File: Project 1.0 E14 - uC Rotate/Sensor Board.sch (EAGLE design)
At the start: 93 parts, among them IC1 LT1963EST-1.5, IC2 LT1963EST-1.5, IC4 LT1963EST-1.5

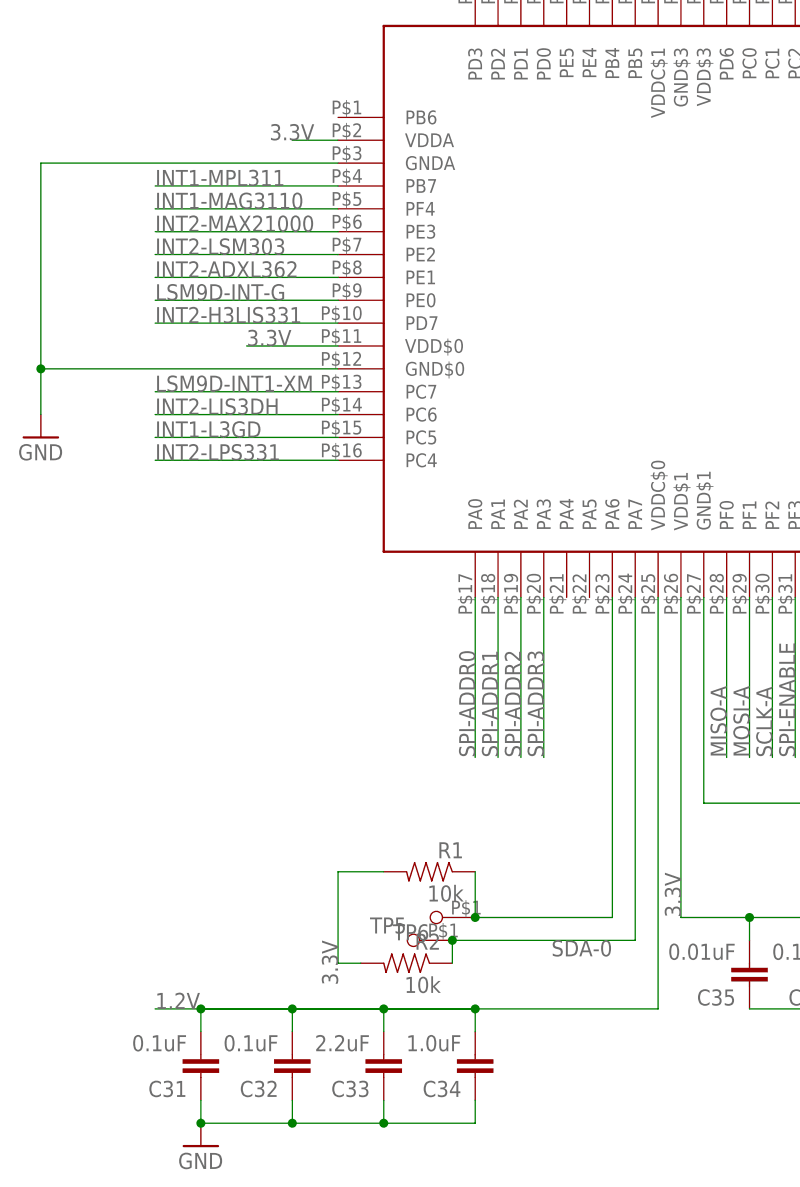
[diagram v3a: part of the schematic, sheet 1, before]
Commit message: All signal connections have been completed. Space has been adequately left between traces to allow for GND plane fill in. Power and GND have not been connected and signal and power trace widths have not been finalised. LSM9DS0 interrupts have not been finalised and may have been incorrectly connected.  LSM9DS0 Gyroscope data enable pin has not been connected since currently it is not clear what its use is or how it is to be used. Gyroscope programmable interrupt pin has been connected but the desired connection may be the gyroscope data ready pin. Also currently there appears to be no interrupt for the magnetometer and this will need to be fixed to enable all 9 axis to be fully used.
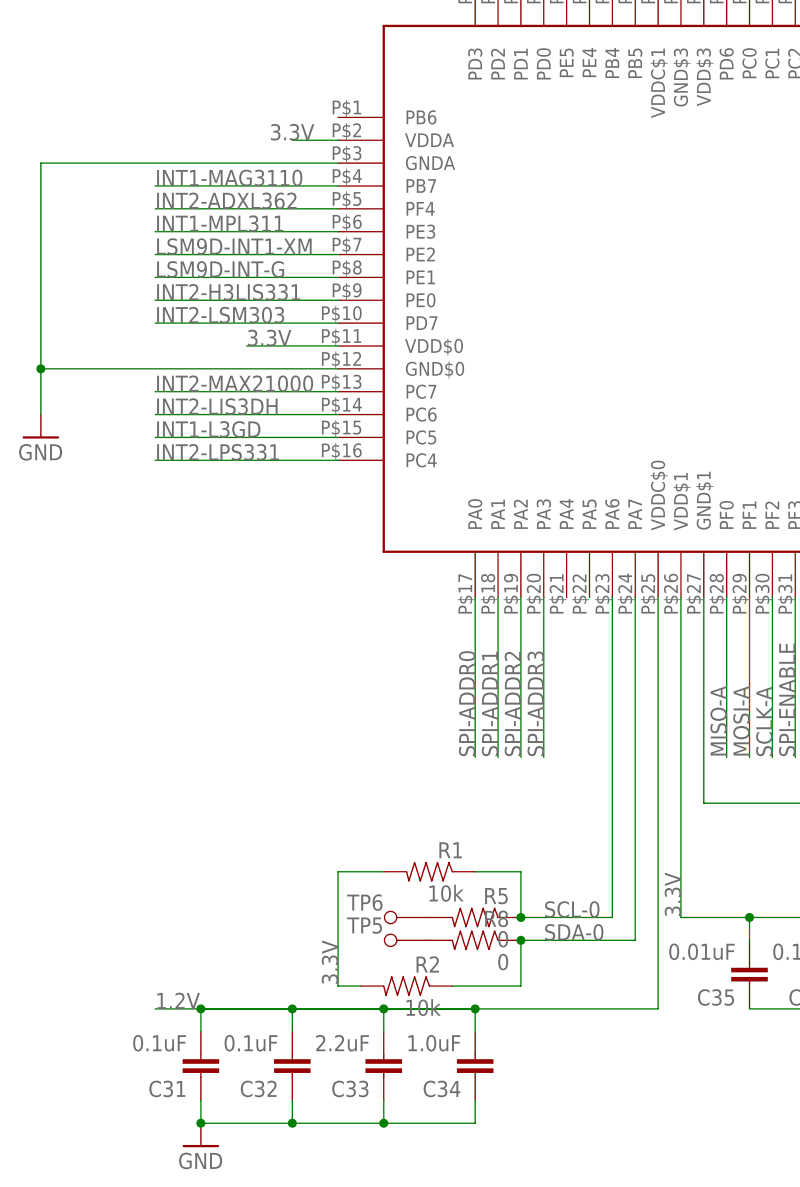
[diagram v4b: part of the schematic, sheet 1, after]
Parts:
- added R5, R8: 0, Kas-Passives:RESISTOR
- TP5, TP6: device Kas-Passives:TESTPAD(ROUND) -> Kas-Connectors:TESTPAD(ROUND)
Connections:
- new net N$24: R5.2, TP6.P$1
- new net N$26: R8.2, TP5.P$1
- net CS-LSM9D30-G: now also U$21.2; no longer U$21.3
- net CS-LSM9DS0-XM: now also U$21.3; no longer U$21.2
- net INT1-MAG3110: now also U$11.PB7; no longer U$11.PF4
- net INT1-MPL311: now also U$11.PE3; no longer U$11.PB7
- net INT2-ADXL362: now also U$11.PF4; no longer U$11.PE1
- net INT2-H3LIS331: now also U$11.PE0; no longer U$11.PD7
- net INT2-LSM303: now also U$11.PD7; no longer U$11.PE2
- net INT2-MAX21000: now also U$11.PC7; no longer U$11.PE3
- net LSM9D-INT-G: now also U$11.PE1; no longer U$11.PE0
- net LSM9D-INT1-XM: now also U$11.PE2; no longer U$11.PC7
- net SCL-0: now also R5.1; no longer TP6.P$1
- net SDA-0: now also R8.1; no longer TP5.P$1
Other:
- moved on the sheet: R2

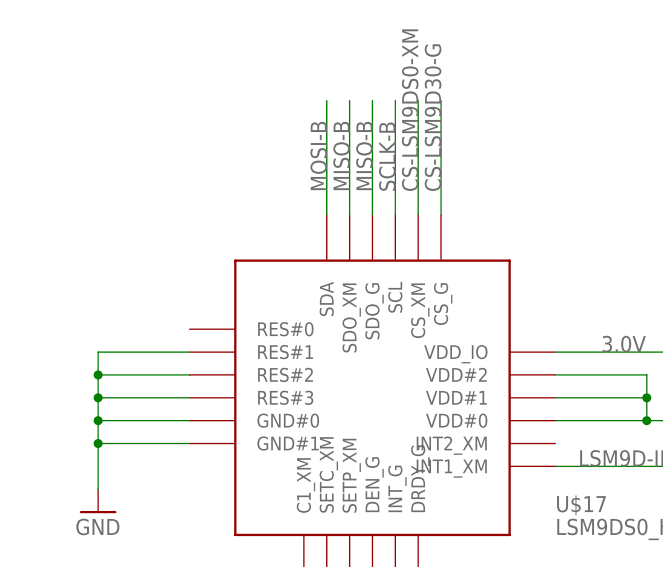
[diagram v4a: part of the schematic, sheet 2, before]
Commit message: Sensor test board: All traces have been confirmed connected except for power and GND. The issues from previous commit remain to be addresed.
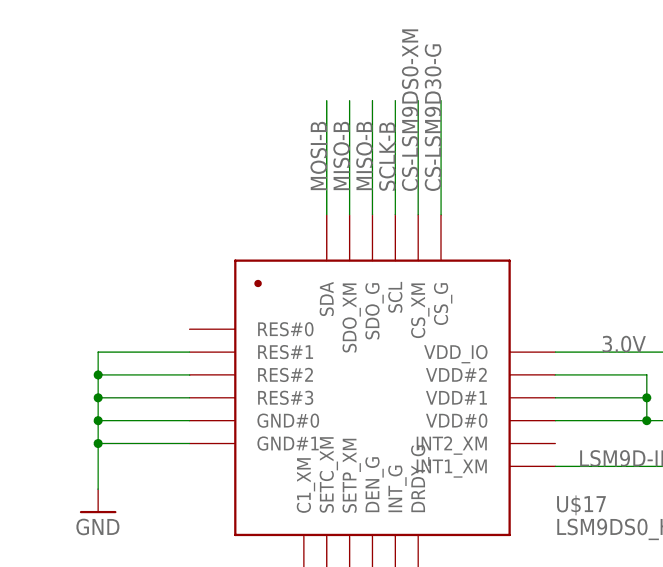
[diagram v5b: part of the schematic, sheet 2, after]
